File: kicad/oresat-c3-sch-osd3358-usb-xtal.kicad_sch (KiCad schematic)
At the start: 42 parts, among them U1 OSD3358-512M-BSM, U11 RCLAMP0504FB, Y1 24MHz, Y2 Crystal

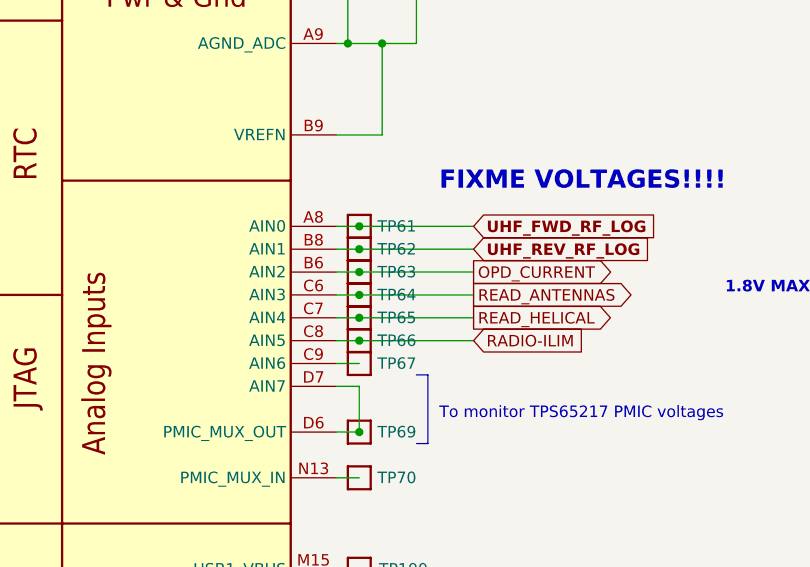
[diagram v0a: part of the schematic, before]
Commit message: Rough draft layout of UHF radio. Fixed duplicated test points.
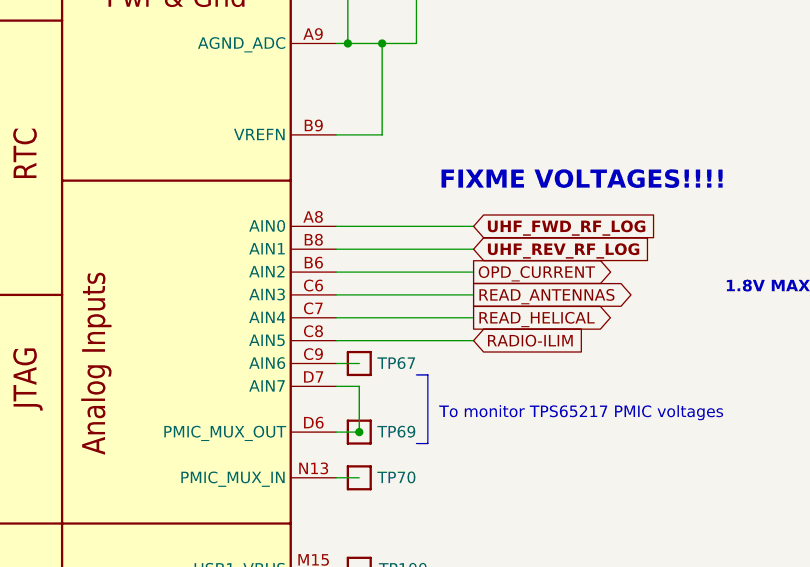
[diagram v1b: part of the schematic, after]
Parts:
- removed TP61, TP62, TP63, TP64, TP65, TP66: Test-Point, oresat-misc:TestPoint_Pad_D1.0mm, symbol oresat-misc:Test-Point-1mm-round
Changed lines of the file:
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@@
   (junction (at 172.72 93.98) (diameter 0) (color 0 0 0 0)
   )
-  (junction (at 259.08 129.54) (diameter 0) (color 0 0 0 0)
-  )
   (junction (at 180.34 162.56) (diameter 0) (color 0 0 0 0)
   )
-  (junction (at 259.08 132.08) (diameter 0) (color 0 0 0 0)
-  )
-  (junction (at 259.08 124.46) (diameter 0) (color 0 0 0 0)
-  )
   (junction (at 179.07 119.38) (diameter 0) (color 0 0 0 0)
   )
@@
   (junction (at 180.34 73.66) (diameter 0) (color 0 0 0 0)
   )
-  (junction (at 259.08 121.92) (diameter 0) (color 0 0 0 0)
-  )
   (junction (at 257.81 101.6) (diameter 0) (color 0 0 0 0)
   )
@@
   )
   (junction (at 167.64 119.38) (diameter 0) (color 0 0 0 0)
-  )
-  (junction (at 259.08 134.62) (diameter 0) (color 0 0 0 0)
-  )
-  (junction (at 259.08 127) (diameter 0) (color 0 0 0 0)
   )
   (junction (at 257.81 81.28) (diameter 0) (color 0 0 0 0)
@@
     (stroke (width 0) (type default))
   )
-  (wire (pts (xy 259.08 129.54) (xy 271.78 129.54))
-    (stroke (width 0) (type default))
-  )
   (wire (pts (xy 193.04 172.72) (xy 195.58 172.72))
     (stroke (width 0) (type default))
@@
     (stroke (width 0) (type default))
   )
-  (wire (pts (xy 256.54 127) (xy 259.08 127))
-    (stroke (width 0) (type default))
-  )
   (wire (pts (xy 215.9 199.39) (xy 215.9 200.66))
     (stroke (width 0) (type default))
@@
     (stroke (width 0) (type default))
   )
-  (wire (pts (xy 256.54 134.62) (xy 259.08 134.62))
+  (wire (pts (xy 256.54 134.62) (xy 271.78 134.62))
     (stroke (width 0) (type default))
   )
@@
     (stroke (width 0) (type default))
   )
-  (wire (pts (xy 256.54 121.92) (xy 259.08 121.92))
-    (stroke (width 0) (type default))
-  )
   (wire (pts (xy 195.58 149.86) (xy 193.04 149.86))
     (stroke (width 0) (type default))
@@
     (stroke (width 0) (type default))
   )
-  (wire (pts (xy 259.08 124.46) (xy 271.78 124.46))
+  (wire (pts (xy 256.54 124.46) (xy 271.78 124.46))
     (stroke (width 0) (type default))
   )
@@
     (stroke (width 0) (type default))
   )
-  (wire (pts (xy 259.08 121.92) (xy 271.78 121.92))
-    (stroke (width 0) (type default))
-  )
-  (wire (pts (xy 256.54 124.46) (xy 259.08 124.46))
+  (wire (pts (xy 256.54 121.92) (xy 271.78 121.92))
     (stroke (width 0) (type default))
   )
@@
     (stroke (width 0) (type default))
   )
-  (wire (pts (xy 259.08 127) (xy 271.78 127))
+  (wire (pts (xy 256.54 127) (xy 271.78 127))
     (stroke (width 0) (type default))
   )
@@
     (stroke (width 0) (type default))
   )
-  (wire (pts (xy 259.08 132.08) (xy 271.78 132.08))
+  (wire (pts (xy 256.54 132.08) (xy 271.78 132.08))
     (stroke (width 0) (type default))
   )
@@
     (stroke (width 0) (type default))
   )
-  (wire (pts (xy 256.54 132.08) (xy 259.08 132.08))
-    (stroke (width 0) (type default))
-  )
-  (wire (pts (xy 256.54 129.54) (xy 259.08 129.54))
-    (stroke (width 0) (type default))
-  )
-  (wire (pts (xy 259.08 134.62) (xy 271.78 134.62))
+  (wire (pts (xy 256.54 129.54) (xy 271.78 129.54))
     (stroke (width 0) (type default))
   )
@@
     )
   )
-  (symbol (lib_id "oresat-misc:Test-Point-1mm-round") (at 259.08 132.08 180) (unit 1)
-    (in_bom yes) (on_board yes) (dnp no)
-    (property "Reference" "TP65" (at 265.43 132.08 0)
-      (effects (font (size 1.27 1.27)) (justify left))
-    )
-    (property "Value" "Test-Point" (at 259.08 134.62 0)
-      (effects (font (size 1.27 1.27)) hide)
-    )
-    (property "Footprint" "oresat-misc:TestPoint_Pad_D1.0mm" (at 259.08 142.24 0)
-      (effects (font (size 1.27 1.27)) hide)
-    )
-    (property "Datasheet" "" (at 259.08 132.08 0)
-      (effects (font (size 1.27 1.27)) hide)
-    )
-    (pin "1")
-    (instances
-      (project "oresat-c3"
-        (path "/65d12cdd-c326-4033-9053-c59fa4e0b25e/0d3a1fa4-c9ee-4335-9068-a81ae0178f3f"
-          (reference "TP65") (unit 1)
-        )
-      )
-    )
-  )
   (symbol (lib_id "Device:Crystal_GND24") (at 166.37 81.28 270) (unit 1)
     (in_bom yes) (on_board yes) (dnp no)
@@
         (path "/65d12cdd-c326-4033-9053-c59fa4e0b25e/0d3a1fa4-c9ee-4335-9068-a81ae0178f3f"
           (reference "TP104") (unit 1)
-        )
-      )
-    )
-  )
-  (symbol (lib_id "oresat-misc:Test-Point-1mm-round") (at 259.08 134.62 180) (unit 1)
-    (in_bom yes) (on_board yes) (dnp no)
-    (property "Reference" "TP66" (at 265.43 134.62 0)
-      (effects (font (size 1.27 1.27)) (justify left))
-    )
-    (property "Value" "Test-Point" (at 259.08 137.16 0)
-      (effects (font (size 1.27 1.27)) hide)
-    )
-    (property "Footprint" "oresat-misc:TestPoint_Pad_D1.0mm" (at 259.08 144.78 0)
-      (effects (font (size 1.27 1.27)) hide)
-    )
-    (property "Datasheet" "" (at 259.08 134.62 0)
-      (effects (font (size 1.27 1.27)) hide)
-    )
-    (pin "1")
-    (instances
-      (project "oresat-c3"
-        (path "/65d12cdd-c326-4033-9053-c59fa4e0b25e/0d3a1fa4-c9ee-4335-9068-a81ae0178f3f"
-          (reference "TP66") (unit 1)
         )
       )
@@
     )
   )
-  (symbol (lib_id "oresat-misc:Test-Point-1mm-round") (at 259.08 121.92 180) (unit 1)
-    (in_bom yes) (on_board yes) (dnp no)
-    (property "Reference" "TP61" (at 265.43 121.92 0)
-      (effects (font (size 1.27 1.27)) (justify left))
-    )
-    (property "Value" "Test-Point" (at 259.08 124.46 0)
-      (effects (font (size 1.27 1.27)) hide)
-    )
-    (property "Footprint" "oresat-misc:TestPoint_Pad_D1.0mm" (at 259.08 132.08 0)
-      (effects (font (size 1.27 1.27)) hide)
-    )
-    (property "Datasheet" "" (at 259.08 121.92 0)
-      (effects (font (size 1.27 1.27)) hide)
-    )
-    (pin "1")
-    (instances
-      (project "oresat-c3"
-        (path "/65d12cdd-c326-4033-9053-c59fa4e0b25e/0d3a1fa4-c9ee-4335-9068-a81ae0178f3f"
-          (reference "TP61") (unit 1)
-        )
-      )
-    )
-  )
   (symbol (lib_id "oresat-misc:Test-Point-1mm-round") (at 259.08 144.78 180) (unit 1)
     (in_bom yes) (on_board yes) (dnp no)
@@
         (path "/65d12cdd-c326-4033-9053-c59fa4e0b25e/0d3a1fa4-c9ee-4335-9068-a81ae0178f3f"
           (reference "TP99") (unit 1)
-        )
-      )
-    )
-  )
-  (symbol (lib_id "oresat-misc:Test-Point-1mm-round") (at 259.08 127 180) (unit 1)
-    (in_bom yes) (on_board yes) (dnp no)
-    (property "Reference" "TP63" (at 265.43 127 0)
-      (effects (font (size 1.27 1.27)) (justify left))
-    )
-    (property "Value" "Test-Point" (at 259.08 129.54 0)
-      (effects (font (size 1.27 1.27)) hide)
-    )
-    (property "Footprint" "oresat-misc:TestPoint_Pad_D1.0mm" (at 259.08 137.16 0)
-      (effects (font (size 1.27 1.27)) hide)
-    )
-    (property "Datasheet" "" (at 259.08 127 0)
-      (effects (font (size 1.27 1.27)) hide)
-    )
-    (pin "1")
-    (instances
-      (project "oresat-c3"
-        (path "/65d12cdd-c326-4033-9053-c59fa4e0b25e/0d3a1fa4-c9ee-4335-9068-a81ae0178f3f"
-          (reference "TP63") (unit 1)
         )
       )
@@
     )
   )
-  (symbol (lib_id "oresat-misc:Test-Point-1mm-round") (at 259.08 124.46 180) (unit 1)
-    (in_bom yes) (on_board yes) (dnp no)
-    (property "Reference" "TP62" (at 265.43 124.46 0)
-      (effects (font (size 1.27 1.27)) (justify left))
-    )
-    (property "Value" "Test-Point" (at 259.08 127 0)
-      (effects (font (size 1.27 1.27)) hide)
-    )
-    (property "Footprint" "oresat-misc:TestPoint_Pad_D1.0mm" (at 259.08 134.62 0)
-      (effects (font (size 1.27 1.27)) hide)
-    )
-    (property "Datasheet" "" (at 259.08 124.46 0)
-      (effects (font (size 1.27 1.27)) hide)
-    )
-    (pin "1")
-    (instances
-      (project "oresat-c3"
-        (path "/65d12cdd-c326-4033-9053-c59fa4e0b25e/0d3a1fa4-c9ee-4335-9068-a81ae0178f3f"
-          (reference "TP62") (unit 1)
-        )
-      )
-    )
-  )
   (symbol (lib_id "Device:C_Small") (at 257.81 91.44 0) (unit 1)
     (in_bom yes) (on_board yes) (dnp no)
@@
         )
       )
-    )
-  )
-  (symbol (lib_id "oresat-misc:Test-Point-1mm-round") (at 259.08 129.54 180) (unit 1)
-    (in_bom yes) (on_board yes) (dnp no)
-    (property "Reference" "TP64" (at 265.43 129.54 0)
-      (effects (font (size 1.27 1.27)) (justify left))
-    )
-    (property "Value" "Test-Point" (at 259.08 132.08 0)
-      (effects (font (size 1.27 1.27)) hide)
-    )
-    (property "Footprint" "oresat-misc:TestPoint_Pad_D1.0mm" (at 259.08 139.7 0)
-      (effects (font (size 1.27 1.27)) hide)
-    )
-    (property "Datasheet" "" (at 259.08 129.54 0)
-      (effects (font (size 1.27 1.27)) hide)
-    )
-    (pin "1")
-    (instances
-      (project "oresat-c3"
-        (path "/65d12cdd-c326-4033-9053-c59fa4e0b25e/0d3a1fa4-c9ee-4335-9068-a81ae0178f3f"
-          (reference "TP64") (unit 1)
-        )
-      )

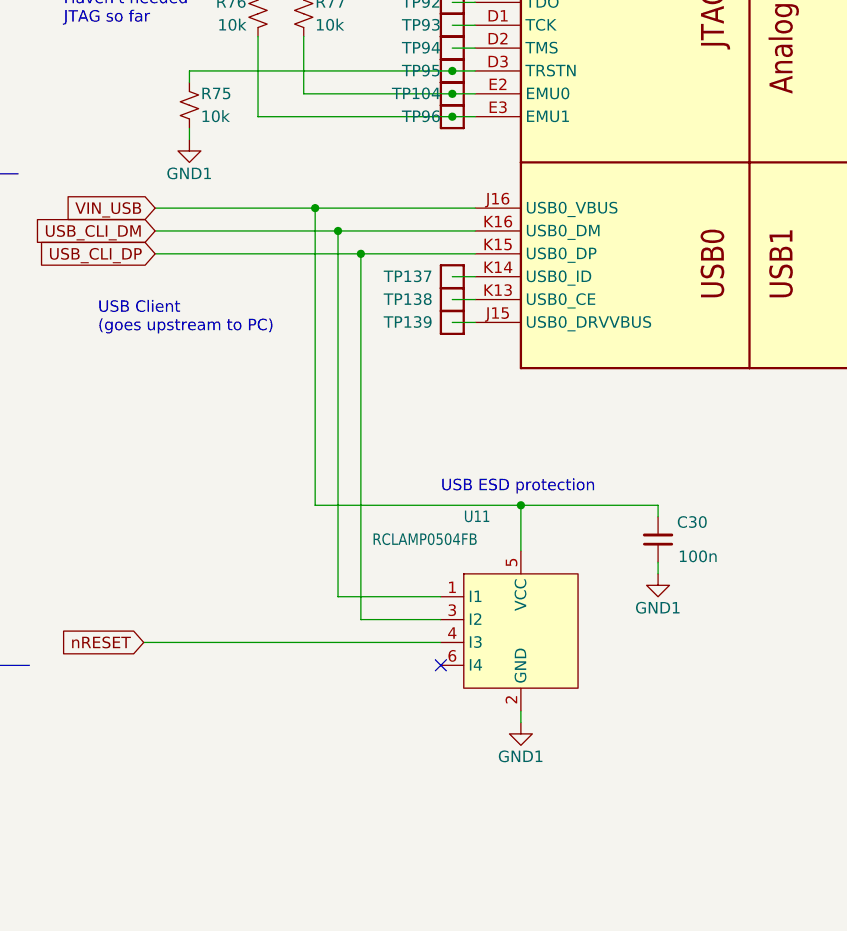
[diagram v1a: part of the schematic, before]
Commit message: Switched all grounds to a single ground, because I can't find a way to overlap ground planes in KiCAD. That's actually not terrible, however, because KiCAD has an anti-plane feature which I used to cut the ground plane between UHF and L radios and L radio and Octavo. So actually I think it came out better than having separate ground planes. Only thing left now are the ~ 40 connections to the Octavo.
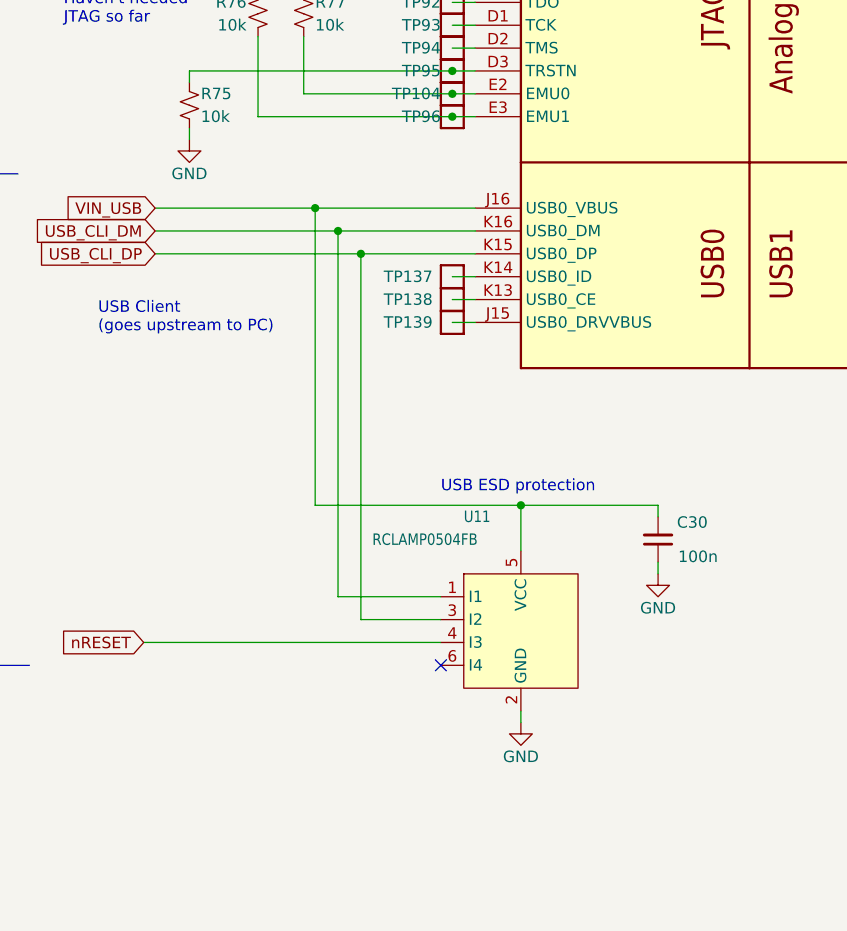
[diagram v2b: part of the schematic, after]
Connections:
- net GND1 renamed GND
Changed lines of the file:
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@@
     )
   )
-  (symbol (lib_id "power:GND1") (at 200.66 217.17 0) (unit 1)
-    (in_bom yes) (on_board yes) (dnp no)
-    (property "Reference" "#PWR0147" (at 200.66 223.52 0)
-      (effects (font (size 1.27 1.27)) hide)
-    )
-    (property "Value" "GND1" (at 200.66 220.98 0)
+  (symbol (lib_id "power:GND") (at 200.66 217.17 0) (unit 1)
+    (in_bom yes) (on_board yes) (dnp no)
+    (property "Reference" "#PWR?" (at 200.66 223.52 0)
+      (effects (font (size 1.27 1.27)) hide)
+    )
+    (property "Value" "GND" (at 200.66 220.98 0)
       (effects (font (size 1.27 1.27)))
     )
@@
       (project "oresat-c3"
         (path "/65d12cdd-c326-4033-9053-c59fa4e0b25e/0d3a1fa4-c9ee-4335-9068-a81ae0178f3f"
-          (reference "#PWR0147") (unit 1)
+          (reference "#PWR?") (unit 1)
         )
       )
@@
     )
   )
-  (symbol (lib_id "power:GND1") (at 163.83 152.4 0) (unit 1)
-    (in_bom yes) (on_board yes) (dnp no)
-    (property "Reference" "#PWR0145" (at 163.83 158.75 0)
-      (effects (font (size 1.27 1.27)) hide)
-    )
-    (property "Value" "GND1" (at 163.83 156.21 0)
+  (symbol (lib_id "power:GND") (at 163.83 152.4 0) (unit 1)
+    (in_bom yes) (on_board yes) (dnp no)
+    (property "Reference" "#PWR?" (at 163.83 158.75 0)
+      (effects (font (size 1.27 1.27)) hide)
+    )
+    (property "Value" "GND" (at 163.83 156.21 0)
       (effects (font (size 1.27 1.27)))
     )
@@
       (project "oresat-c3"
         (path "/65d12cdd-c326-4033-9053-c59fa4e0b25e/0d3a1fa4-c9ee-4335-9068-a81ae0178f3f"
-          (reference "#PWR0145") (unit 1)
+          (reference "#PWR?") (unit 1)
         )
       )
@@
     )
   )
-  (symbol (lib_id "power:GND1") (at 215.9 200.66 0) (unit 1)
-    (in_bom yes) (on_board yes) (dnp no)
-    (property "Reference" "#PWR0146" (at 215.9 207.01 0)
-      (effects (font (size 1.27 1.27)) hide)
-    )
-    (property "Value" "GND1" (at 215.9 204.47 0)
+  (symbol (lib_id "power:GND") (at 215.9 200.66 0) (unit 1)
+    (in_bom yes) (on_board yes) (dnp no)
+    (property "Reference" "#PWR?" (at 215.9 207.01 0)
+      (effects (font (size 1.27 1.27)) hide)
+    )
+    (property "Value" "GND" (at 215.9 204.47 0)
       (effects (font (size 1.27 1.27)))
     )
@@
       (project "oresat-c3"
         (path "/65d12cdd-c326-4033-9053-c59fa4e0b25e/0d3a1fa4-c9ee-4335-9068-a81ae0178f3f"
-          (reference "#PWR0146") (unit 1)
-        )
-      )
+          (reference "#PWR?") (unit 1)
+        )
+      )

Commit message: Zero airwires! Rough draft schematic and layout are done. Still need ERC and DRC and full design review and stiching and polish.
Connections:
- net RADIO-ILIM is gone; now on net READ_HELICAL: U1.C8 (AIN5)
- net READ_ANTENNAS: now also U1.C7 (AIN4); no longer U1.C6 (AIN3)
- net READ_HELICAL: no longer U1.C7 (AIN4)
- new net RADIO_ILIM: U1.C6 (AIN3)
